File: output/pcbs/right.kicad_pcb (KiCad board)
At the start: 2 copper layers, 139.8 x 121.8 mm, 63 parts

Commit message: wip routing right board
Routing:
- net P029: track 0.00 -> 125.6 mm, vias 0 -> 1
- net P115: track 0.00 -> 25.9 mm
- net P113: track 0.00 -> 25.9 mm
- net P002: track 0.00 -> 25.9 mm
- net mirror_fourth_mod: track 0.00 -> 24.3 mm
- net mirror_fourth_home: track 0.00 -> 23.6 mm
- net mirror_third_top: track 0.00 -> 23.1 mm
- net mirror_third_home: track 0.00 -> 22.9 mm
- net mirror_near_thumb: track 0.00 -> 22.9 mm
- net mirror_first_mod: track 0.00 -> 22.9 mm
- net mirror_second_bottom: track 0.00 -> 22.8 mm
- net mirror_fourth_top: track 0.00 -> 22.7 mm
- net mirror_first_home: track 0.00 -> 22.7 mm
- net mirror_third_mod: track 0.00 -> 22.7 mm
- net mirror_third_bottom: track 0.00 -> 22.7 mm
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
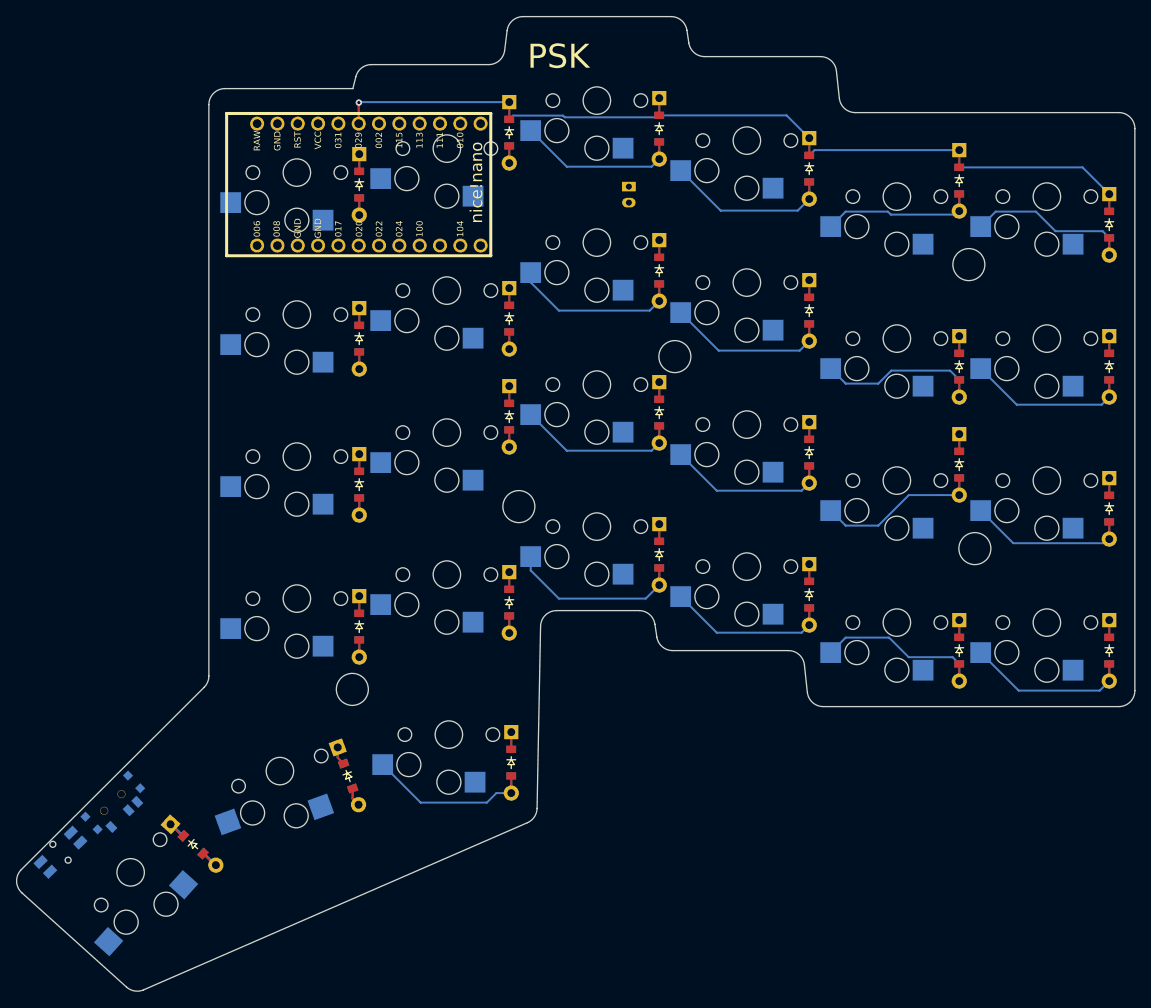
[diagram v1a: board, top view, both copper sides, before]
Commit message: routed left and right, DRC passed
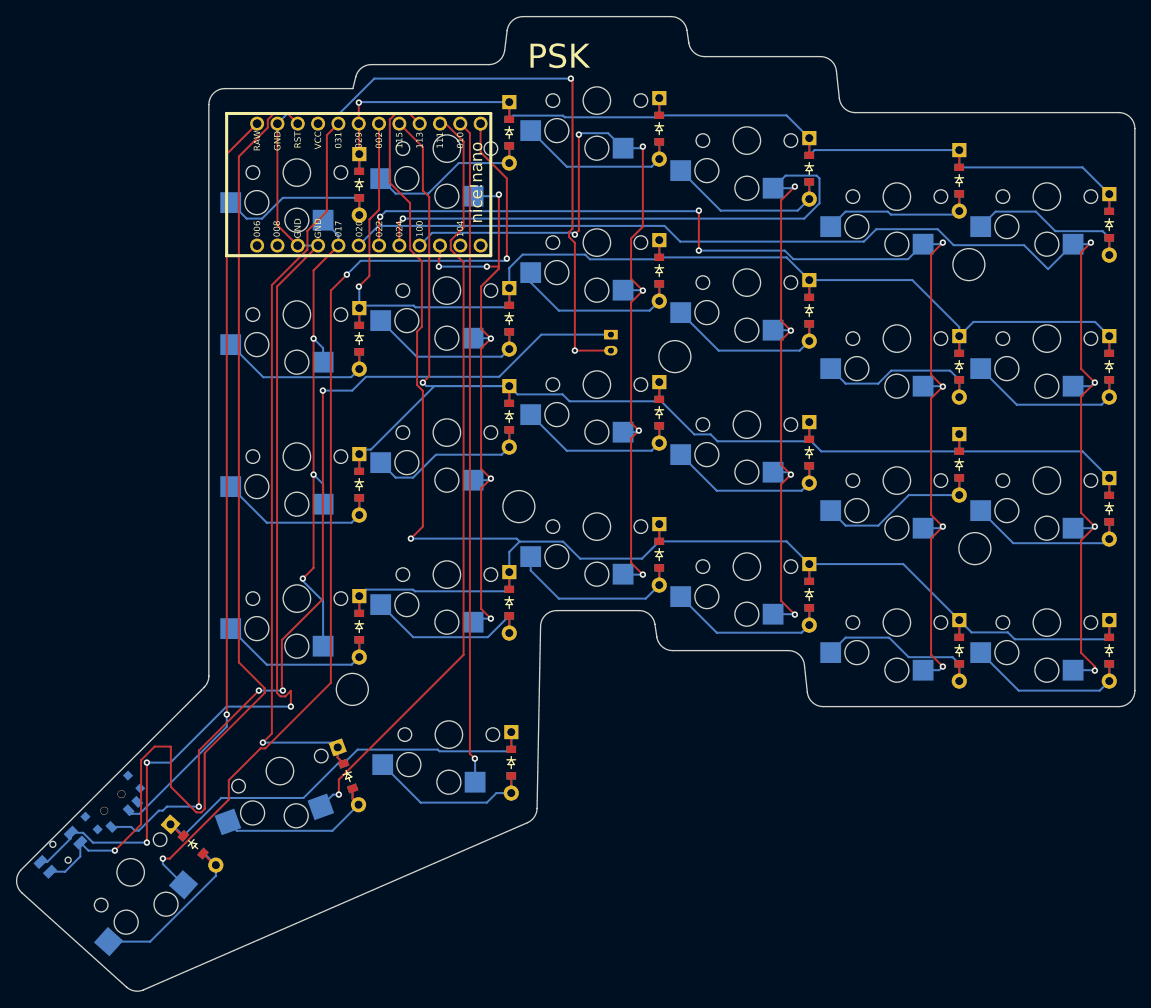
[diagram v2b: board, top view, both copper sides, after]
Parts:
- moved JST1 18.6 mm to (333.0, 115.0)
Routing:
- net GND: track 0.00 -> 205.7 mm, vias 0 -> 5
- net P113: track 25.9 -> 203.7 mm, vias 0 -> 1
- net P020: track 0.00 -> 163.5 mm, vias 0 -> 4
- net P115: track 25.9 -> 173.6 mm, vias 0 -> 1
- net P022: track 0.00 -> 145.0 mm, vias 0 -> 7
- net P031: track 13.4 -> 149.9 mm, vias 0 -> 1
- net RST: track 0.00 -> 135.5 mm, vias 0 -> 1
- net P024: track 0.00 -> 133.2 mm, vias 0 -> 5
- net P002: track 25.9 -> 153.9 mm, vias 0 -> 1
- net P009: track 0.00 -> 126.8 mm, vias 0 -> 3
- net pos: track 0.00 -> 111.5 mm, vias 0 -> 4
- net P100: track 0.00 -> 105.6 mm, vias 0 -> 6
- net P111: track 0.00 -> 96.2 mm, vias 0 -> 1
- net RAW: track 0.00 -> 93.9 mm, vias 0 -> 1
- net P010: track 0.00 -> 83.1 mm, vias 0 -> 1
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
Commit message: generated gerber files, sent off for fab
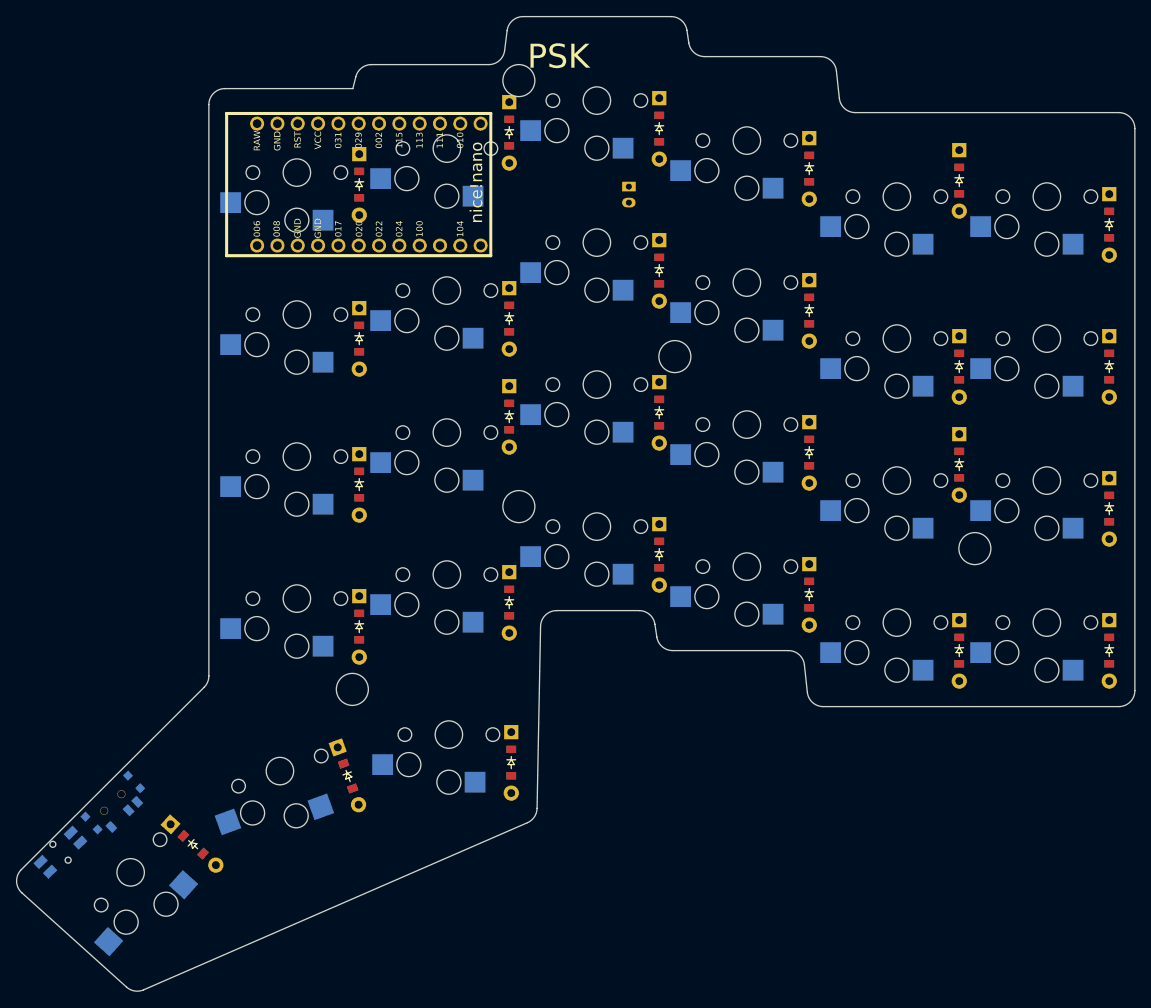
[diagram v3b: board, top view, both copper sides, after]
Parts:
- removed the ? at (300.7, 158.3)
- removed the ? at (377.8, 105.2)
- added ?: , HOLE_M2_TH, F.Cu at (321.5, 82.2)
- added ?: , HOLE_M2_TH, F.Cu at (300.7, 158.3)
- moved JST1 18.6 mm to (335.2, 96.5)
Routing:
- net GND: track 205.7 -> 0.00 mm, vias 5 -> 0
- net P113: track 203.7 -> 0.00 mm, vias 1 -> 0
- net P115: track 173.6 -> 0.00 mm, vias 1 -> 0
- net P020: track 163.5 -> 0.00 mm, vias 4 -> 0
- net P002: track 153.9 -> 0.00 mm, vias 1 -> 0
- net P031: track 149.9 -> 0.00 mm, vias 1 -> 0
- net P022: track 145.0 -> 0.00 mm, vias 7 -> 0
- net RST: track 135.5 -> 0.00 mm, vias 1 -> 0
- net P024: track 133.2 -> 0.00 mm, vias 5 -> 0
- net P029: track 129.4 -> 0.00 mm, vias 1 -> 0
- net P009: track 126.8 -> 0.00 mm, vias 3 -> 0
- net pos: track 111.5 -> 0.00 mm, vias 4 -> 0
- net P100: track 105.6 -> 0.00 mm, vias 6 -> 0
- net P111: track 96.2 -> 0.00 mm, vias 1 -> 0
- net RAW: track 93.9 -> 0.00 mm, vias 1 -> 0
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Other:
- outline, holes or cut-outs redrawn
- net class Default added: clearance 0.2, trace_width 0.25, via_dia 0.8, via_drill 0.4
